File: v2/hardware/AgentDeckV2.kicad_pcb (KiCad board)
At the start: 2 copper layers, 150 x 110 mm, 126 parts, among them J1 USB-C_SMD-TYPE-C-31-M-12_1, J2 JST_PH_S2B-PH-SM4-TB_1x02-1MP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, J3 SWD, Q1 SOT-23, SW1 ChocV1_Direct, SW10 ChocV1_Direct, SW11 ChocV1_Direct, SW12 ChocV1_Direct, SW13 ChocV1_Direct, SW14 ChocV1_Direct, SW15 ChocV1_Direct, SW16 ChocV1_Direct, SW17 ChocV1_Direct, SW18 ChocV1_Direct, SW19 ChocV1_Direct, SW2 ChocV1_Direct, SW20 ChocV1_Direct, SW25 MSK12C02, SW26 SW-SMD_4P-L5.1-W5.1-P3.70-LS6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, SW27 SW-SMD_4P-L5.1-W5.1-P3.70-LS6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, SW3 ChocV1_Direct, SW4 ChocV1_Direct, SW5 ChocV1_Direct, SW6 ChocV1_Direct, SW7 ChocV1_Direct, SW8 ChocV1_Direct, SW9 ChocV1_Direct, U1 WIRELM-SMD_ESP32-S3-WROOM-1, U2 SOT-23-5_L3.0-W1.7-P0.95-LS2.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, U3 SOT-23-6_L2.9-W1.6-P0.95-LS2.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, U4 ESOP-8_TP4056, U5 SOT-23-5_L3.0-W1.7-P0.95-LS2.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

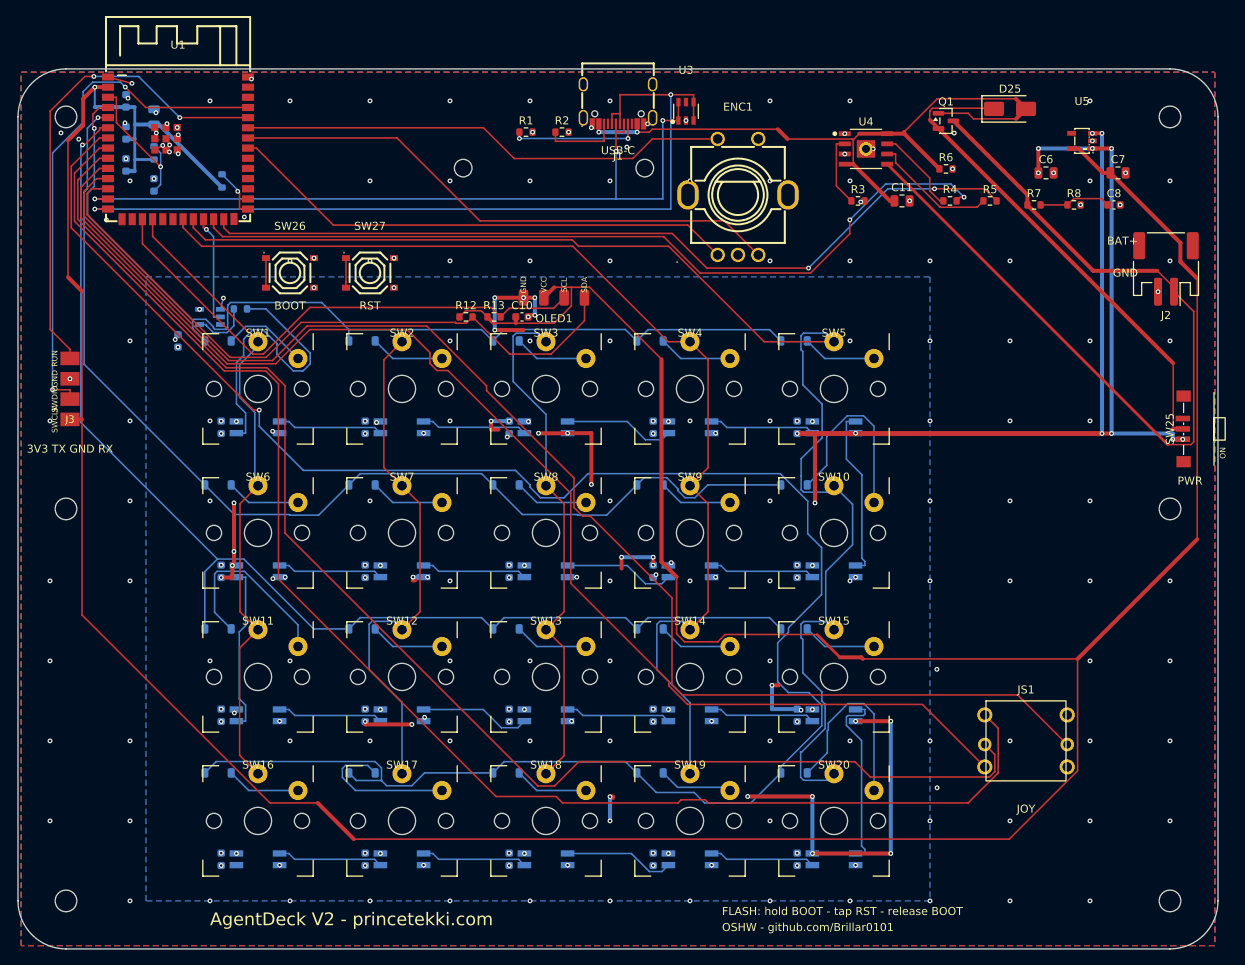
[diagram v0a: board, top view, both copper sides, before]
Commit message: strip v2 routing
Placement-only board for hand routing: all tracks, vias and copper pours
removed (799 tracks, 306 vias, 3 zones). The autorouted version stays in
history at f1eb7db. Keepouts, outline, holes and silk untouched.

Claude-Session: https://claude.ai/code/session_01GWeFSftAaDQLi7MhELLoa4
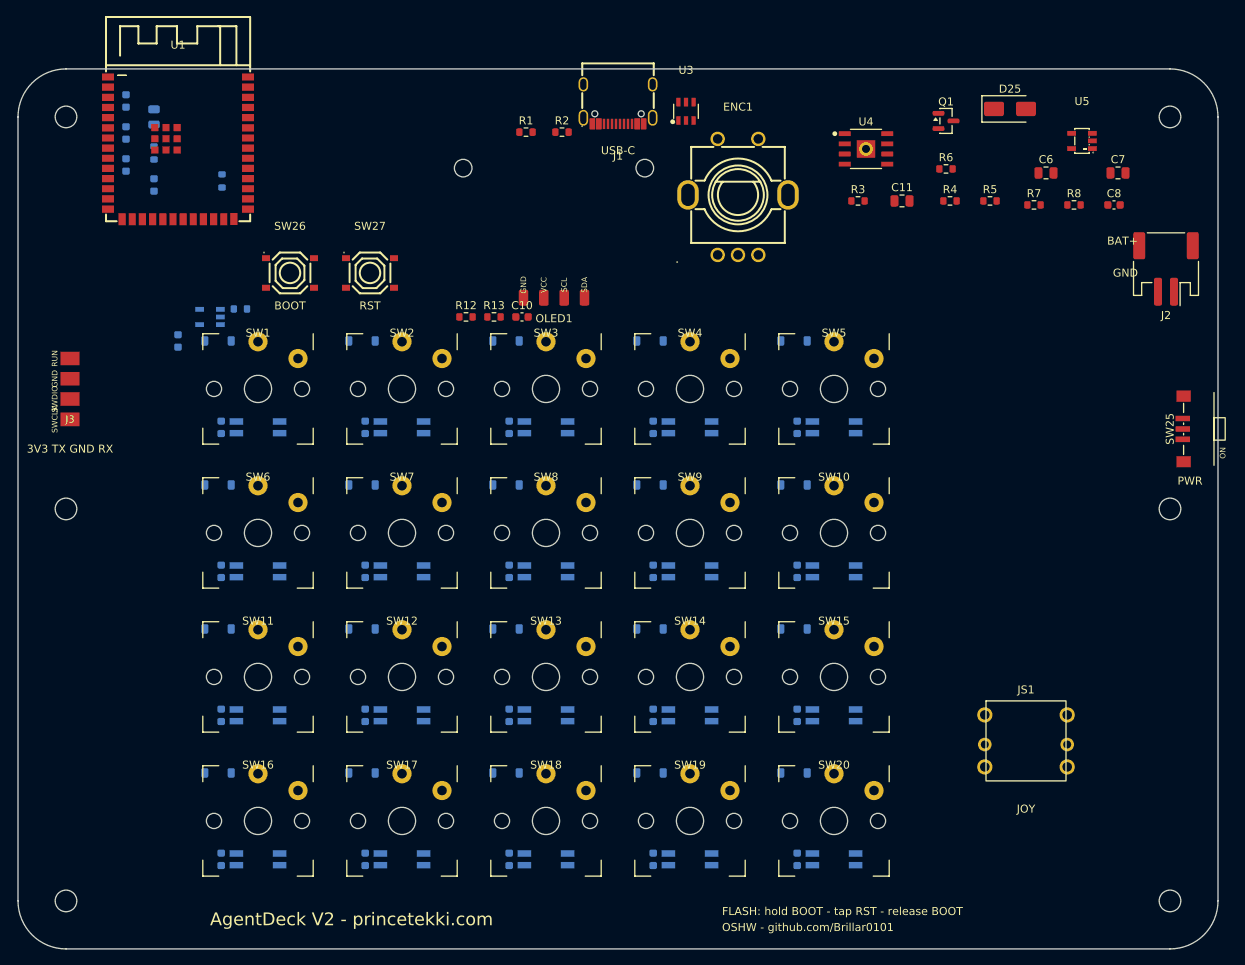
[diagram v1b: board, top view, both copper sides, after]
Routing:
- net +3V3: track 461.9 -> 0.00 mm, vias 1 -> 0
- net VSYS_SW: track 274.3 -> 0.00 mm, vias 62 -> 0
- net ROW3: track 250.9 -> 0.00 mm, vias 1 -> 0
- net JOY_UP: track 181.2 -> 0.00 mm
- net JOY_LEFT: track 170.8 -> 0.00 mm
- net JOY_RIGHT: track 169.4 -> 0.00 mm
- net COL4: track 168.2 -> 0.00 mm
- net JOY_DOWN: track 160.8 -> 0.00 mm
- net ROW2: track 150.1 -> 0.00 mm, vias 1 -> 0
- net ROW1: track 135.8 -> 0.00 mm, vias 1 -> 0
- net COL3: track 135.2 -> 0.00 mm
- net ROW0: track 120.0 -> 0.00 mm, vias 1 -> 0
- net BAT+: track 110.2 -> 0.00 mm
- net USB_DP: track 106.3 -> 0.00 mm, vias 2 -> 0
- net CHRG_SNS: track 104.7 -> 0.00 mm, vias 2 -> 0
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- removed copper zone on B.Cu, net GND
- removed copper zone on F.Cu, net GND
- removed copper zone on B.Cu, net VSYS_SW
